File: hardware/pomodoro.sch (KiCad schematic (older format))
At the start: 23 parts, among them IC1 ATMEGA328-P, SW1 RESET, SW2 SW_PUSH, U1 7805, X1 16 MHz

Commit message: still wrestling with the schematic.
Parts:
- removed C1, C2: 10 uF, symbol C
- added C1, C2: 10 uF, symbol CP1
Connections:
- net +5V: now also C1.1
- net GND: now also D2.2 (K), D3.2 (K), D4.2 (K), D5.2 (K), D6.2 (K), R8.1, C1.2, C2.2; no longer R8.2
- net at IC1.20 (AVCC), IC1.21 (AREF), IC1.7 (VCC)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: now also C2.1
- net at IC1.4 ((PCINT18/INT0)PD2), SW2.1: now also R8.2; no longer R8.1
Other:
- moved on the sheet: C3, C4, D1, D2, D3, D4, D5, D6, IC1, R1, R2, R3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

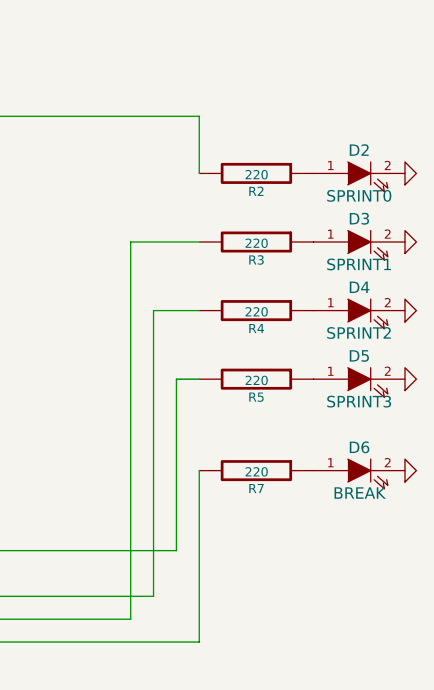
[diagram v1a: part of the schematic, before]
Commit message: need to reconfigure led output pins
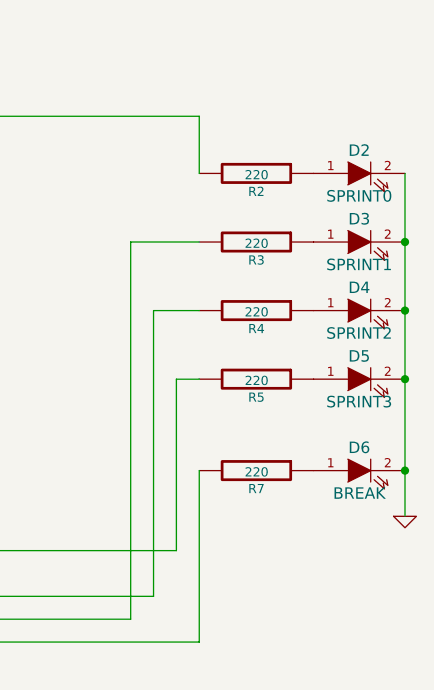
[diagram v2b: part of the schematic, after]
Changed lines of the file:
@@
 L GND #PWR13
 U 1 1 56E41398
-P 8550 4650
-F 0 "#PWR13" H 8550 4650 30  0001 C CNN
-F 1 "GND" H 8550 4580 30  0001 C CNN
-F 2 "" H 8550 4650 60  0000 C CNN
-F 3 "" H 8550 4650 60  0000 C CNN
-	1    8550 4650
-	0    -1   -1   0
-$EndComp
-$Comp
-L GND #PWR12
-U 1 1 56E413AA
-P 8550 4250
-F 0 "#PWR12" H 8550 4250 30  0001 C CNN
-F 1 "GND" H 8550 4180 30  0001 C CNN
-F 2 "" H 8550 4250 60  0000 C CNN
-F 3 "" H 8550 4250 60  0000 C CNN
-	1    8550 4250
-	0    -1   -1   0
-$EndComp
-$Comp
-L GND #PWR10
-U 1 1 56E413B5
-P 8550 3950
-F 0 "#PWR10" H 8550 3950 30  0001 C CNN
-F 1 "GND" H 8550 3880 30  0001 C CNN
-F 2 "" H 8550 3950 60  0000 C CNN
-F 3 "" H 8550 3950 60  0000 C CNN
-	1    8550 3950
-	0    -1   -1   0
-$EndComp
-$Comp
-L GND #PWR9
-U 1 1 56E413C0
-P 8550 3650
-F 0 "#PWR9" H 8550 3650 30  0001 C CNN
-F 1 "GND" H 8550 3580 30  0001 C CNN
-F 2 "" H 8550 3650 60  0000 C CNN
-F 3 "" H 8550 3650 60  0000 C CNN
-	1    8550 3650
-	0    -1   -1   0
-$EndComp
-$Comp
-L GND #PWR8
-U 1 1 56E413CB
-P 8550 3350
-F 0 "#PWR8" H 8550 3350 30  0001 C CNN
-F 1 "GND" H 8550 3280 30  0001 C CNN
-F 2 "" H 8550 3350 60  0000 C CNN
-F 3 "" H 8550 3350 60  0000 C CNN
-	1    8550 3350
-	0    -1   -1   0
+P 8550 4850
+F 0 "#PWR13" H 8550 4850 30  0001 C CNN
+F 1 "GND" H 8550 4780 30  0001 C CNN
+F 2 "" H 8550 4850 60  0000 C CNN
+F 3 "" H 8550 4850 60  0000 C CNN
+	1    8550 4850
+	1    0    0    -1
 $EndComp
 $Comp
@@
 	1    0    0    -1
 $EndComp
+Wire Wire Line
+	8550 3350 8550 4850
+Connection ~ 8550 4650
+Connection ~ 8550 4250
+Connection ~ 8550 3950
+Connection ~ 8550 3650
 $EndSCHEMATC

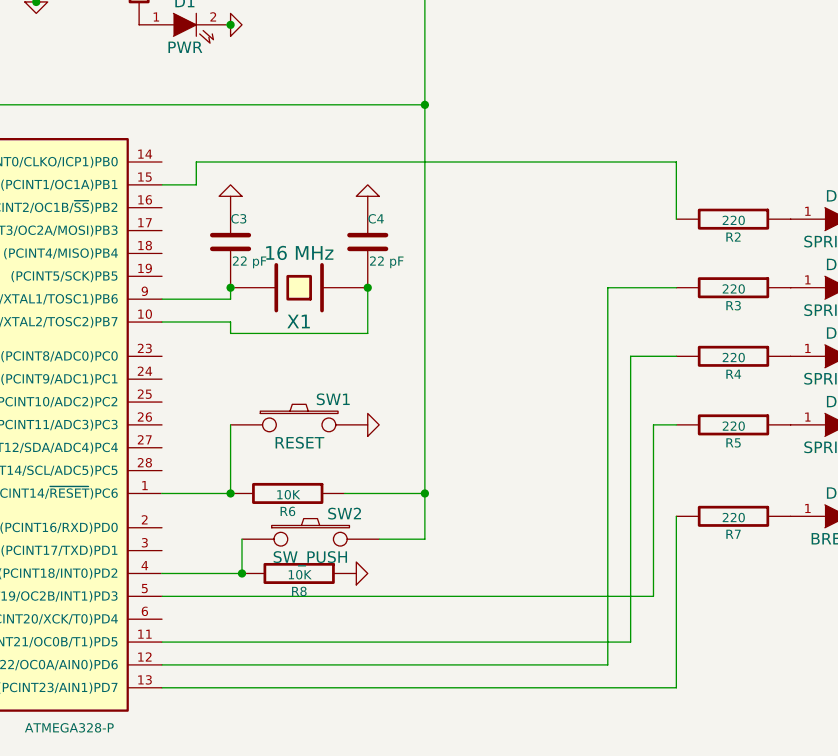
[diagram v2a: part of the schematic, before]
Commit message: repinned the LEDs to prevent needing to use jumpers on PCB
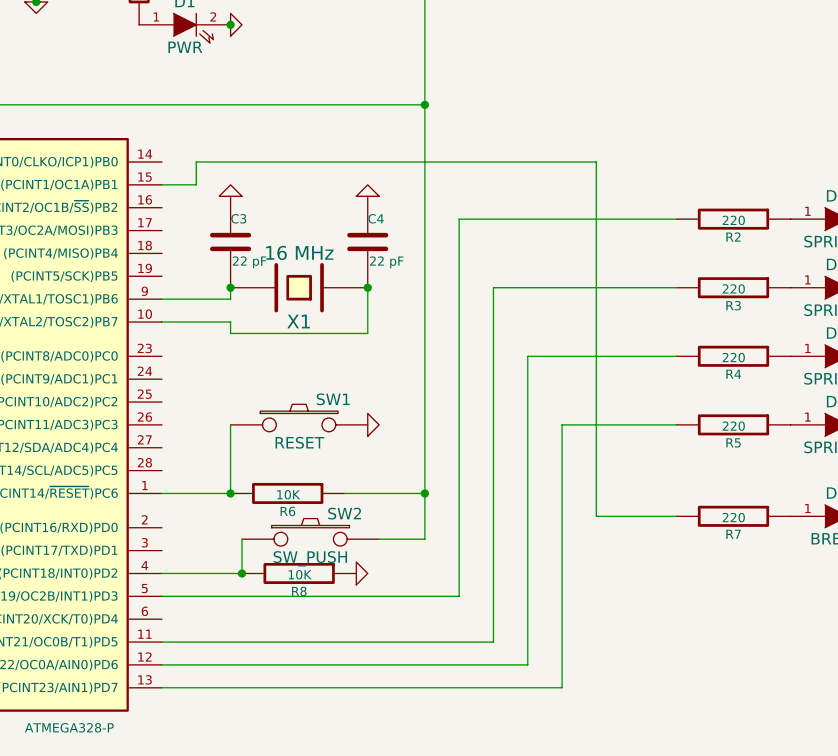
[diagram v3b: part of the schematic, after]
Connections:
- net at IC1.11 ((PCINT21/OC0B/T1)PD5): now also R3.2; no longer R4.2
- net at IC1.12 ((PCINT22/OC0A/AIN0)PD6): now also R4.2; no longer R3.2
- net at IC1.13 ((PCINT23/AIN1)PD7): now also R5.2; no longer R7.2
- net at IC1.15 ((PCINT1/OC1A)PB1): now also R7.2; no longer R2.2
- net at IC1.5 ((PCINT19/OC2B/INT1)PD3): now also R2.2; no longer R5.2
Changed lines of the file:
@@
 Connection ~ 6300 3650
-Wire Wire Line
-	5400 5400 7650 5400
-Wire Wire Line
-	7650 5400 7650 4650
-Wire Wire Line
-	5400 5000 7550 5000
-Wire Wire Line
-	7550 5000 7550 4250
-Wire Wire Line
-	7550 4250 7650 4250
-Wire Wire Line
-	5400 5200 7450 5200
-Wire Wire Line
-	7450 5200 7450 3950
-Wire Wire Line
-	7450 3950 7650 3950
-Wire Wire Line
-	5400 5300 7350 5300
-Wire Wire Line
-	7350 5300 7350 3650
-Wire Wire Line
-	7350 3650 7650 3650
 Wire Wire Line
 	5400 3200 5550 3200
 Wire Wire Line
 	5550 3200 5550 3100
-Wire Wire Line
-	5550 3100 7650 3100
-Wire Wire Line
-	7650 3100 7650 3350
 $Comp
 L SW_PUSH SW2
@@
 Connection ~ 8550 3950
 Connection ~ 8550 3650
+Wire Wire Line
+	5400 5000 6700 5000
+Wire Wire Line
+	6700 5000 6700 3350
+Wire Wire Line
+	6700 3350 7650 3350
+Wire Wire Line
+	5400 5200 6850 5200
+Wire Wire Line
+	6850 5200 6850 3650
+Wire Wire Line
+	6850 3650 7650 3650
+Wire Wire Line
+	5400 5300 7000 5300
+Wire Wire Line
+	7000 5300 7000 3950
+Wire Wire Line
+	7000 3950 7650 3950
+Wire Wire Line
+	5400 5400 7150 5400
+Wire Wire Line
+	7150 5400 7150 4250
+Wire Wire Line
+	7150 4250 7650 4250
+Wire Wire Line
+	5550 3100 7300 3100
+Wire Wire Line
+	7300 3100 7300 4650
+Wire Wire Line
+	7300 4650 7650 4650
 $EndSCHEMATC

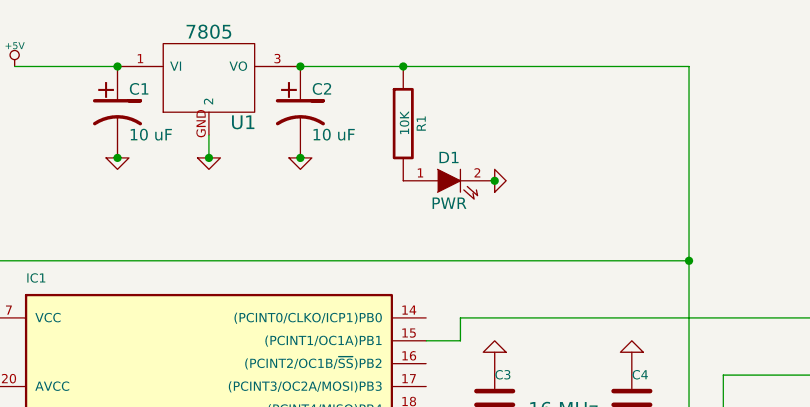
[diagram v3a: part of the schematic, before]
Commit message: fixed power led resistor value
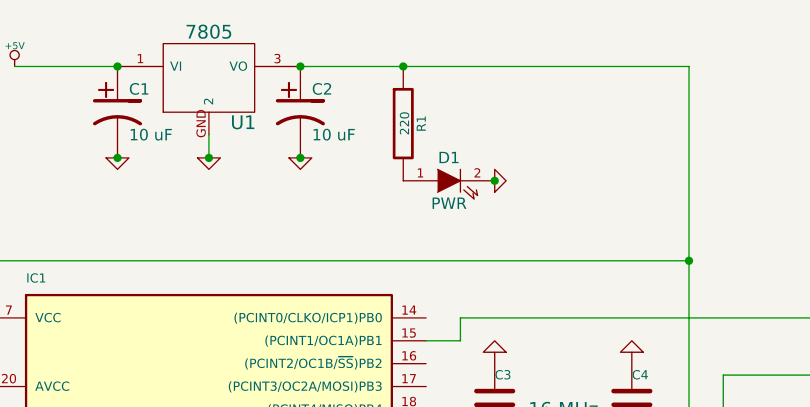
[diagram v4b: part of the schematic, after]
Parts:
- R1: value 10K -> 220
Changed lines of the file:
@@
 P 5300 2250
 F 0 "R1" V 5380 2250 40  0000 C CNN
-F 1 "10K" V 5307 2251 40  0000 C CNN
+F 1 "220" V 5307 2251 40  0000 C CNN
 F 2 "" V 5230 2250 30  0000 C CNN
 F 3 "" H 5300 2250 30  0000 C CNN
